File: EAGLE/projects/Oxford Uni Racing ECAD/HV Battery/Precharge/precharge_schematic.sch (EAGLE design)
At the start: 38 parts, among them IC1 TLV313QDCKRQ1, IC2 TLV313QDCKRQ1, U1 AMC1350QDWVRQ1AMC1350QDWVRQ1_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

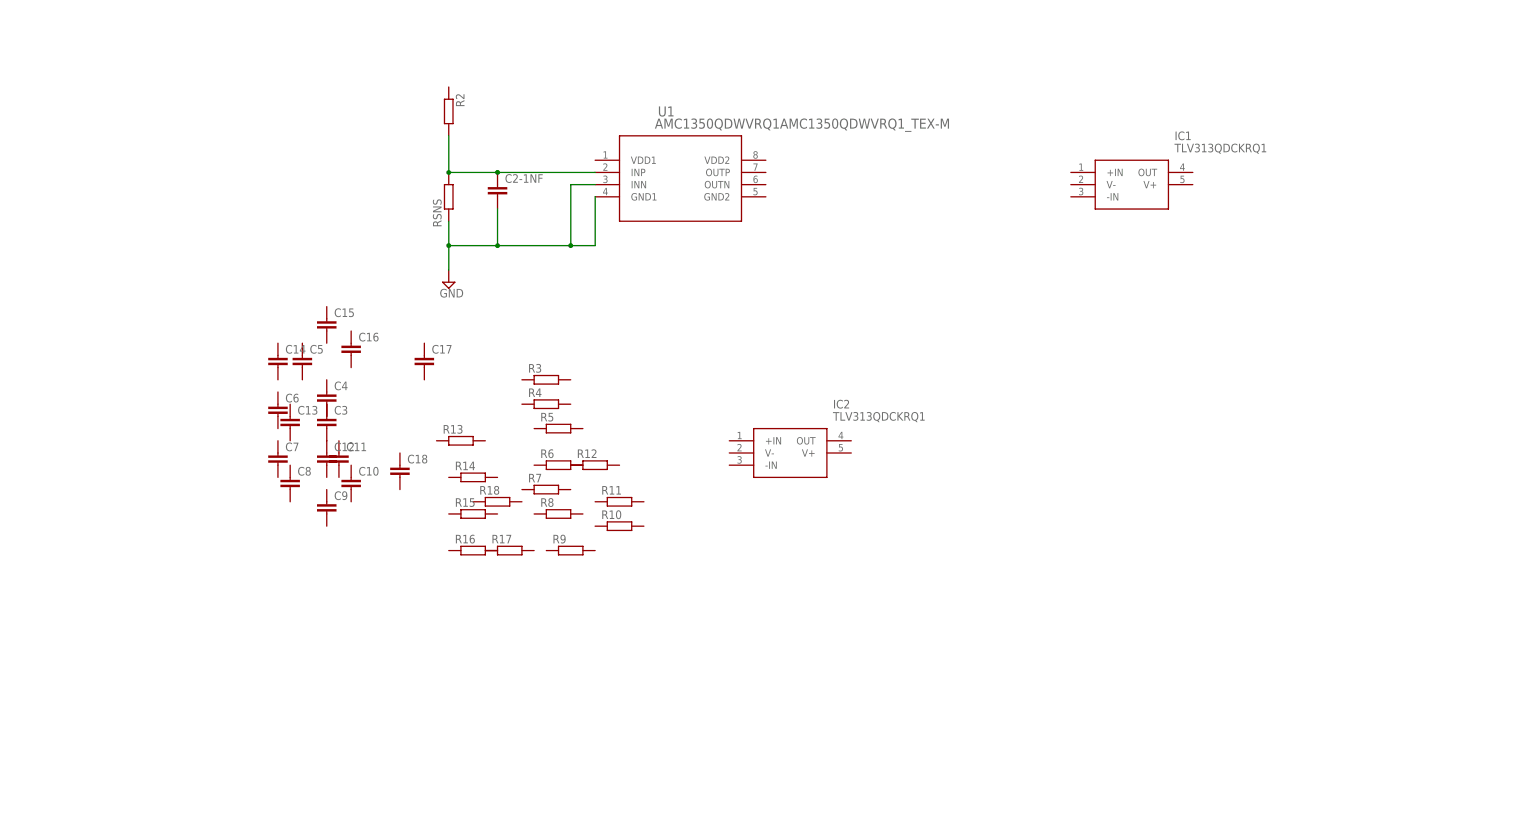
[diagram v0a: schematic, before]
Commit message: precharge board/ main board transfer
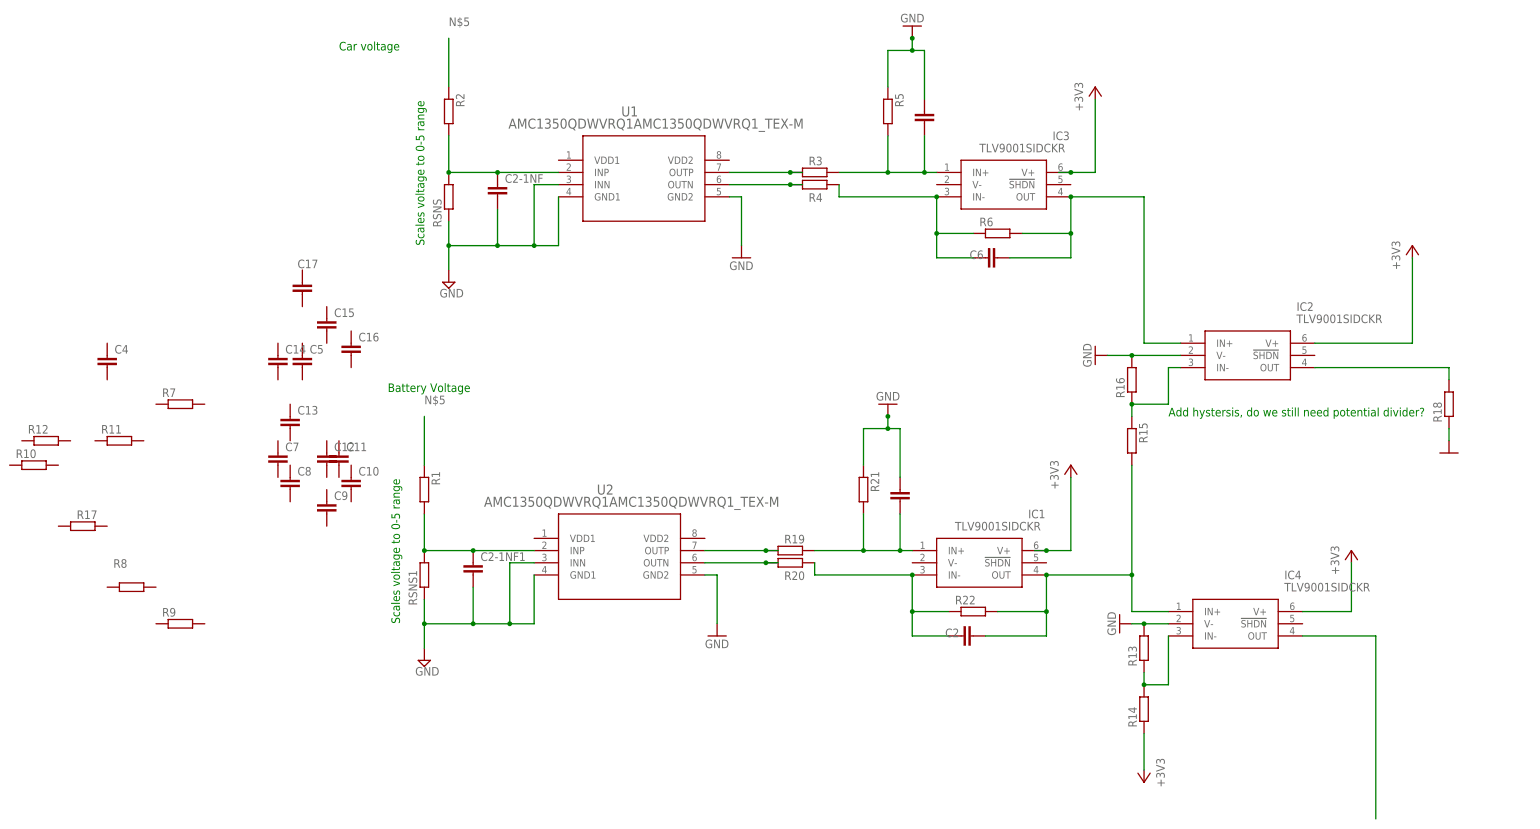
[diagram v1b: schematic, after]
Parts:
- removed C18: (no value), rcl:C-EUC0805
- added C1, C2, C2-1NF1: (no value), rcl:C-EUC0805
- added IC3, IC4: TLV9001SIDCKR, TLV9001SIDCKR:TLV9001SIDCKR
- added R1, R19, R20, R21, R22, RSNS1: (no value), rcl:R-EU_R0805
- added U2: AMC1350QDWVRQ1AMC1350QDWVRQ1_TEX-M, AMC1350QDWVRQ1:AMC1350QDWVRQ1AMC1350QDWVRQ1_TEX-M
- IC1, IC2: value TLV313QDCKRQ1 -> TLV9001SIDCKR; device TLV313QDCKRQ1:TLV313QDCKRQ1 -> TLV9001SIDCKR:TLV9001SIDCKR
- U1: MANUFACTURER_PART_NUMBER (none) -> AMC1350
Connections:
- new net +3V3: IC1.V+, IC2.V+, IC3.V+, IC4.V+, R14.1
- new net N$10: R19.1, U2.OUTP
- new net N$11: R20.1, U2.OUTN
- new net N$12: C1.2, IC1.IN+, R19.2, R21.2
- new net N$13: C1.1, R21.1
- new net N$14: C2.1, IC1.IN-, R20.2, R22.1
- new net N$15: IC2.OUT, R18.2
- new net N$16: C2.2, IC1.OUT, IC2.IN-, IC4.IN+, R15.1, R15.2, R16.1, R22.2
- new net N$17: IC4.IN-, R13.1, R14.2
- new net N$19: IC4.OUT
- new net N$3: R4.1, U1.OUTN
- new net N$4: R3.1, U1.OUTP
- new net N$5: R1.1, R2.1
- new net N$6: C3.2, IC3.IN+, R3.2, R5.2
- new net N$7: C6.1, IC3.IN-, R4.2, R6.1
- new net N$8: C6.2, IC2.IN+, IC3.OUT, R6.2
- new net N$9: C2-1NF1.1, R1.2, RSNS1.2, U2.INP
- net GND: now also C2-1NF1.2, IC2.V-, IC4.V-, R13.2, R16.2, R18.1, RSNS1.1, U1.GND2, U2.GND1, U2.GND2, U2.INN
- net N$2: now also C3.1, R5.1; no longer C12.1, C3.2
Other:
- note added: "Add hystersis, do we still need potential divider?"
- note added: "Battery Voltage"
- note added: "Car voltage"
- note added: "Scales voltage to 0-5 range"
- moved on the sheet: C17, C4, C6, R10, R11, R12, R13, R14, R15, R16, R17, R18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

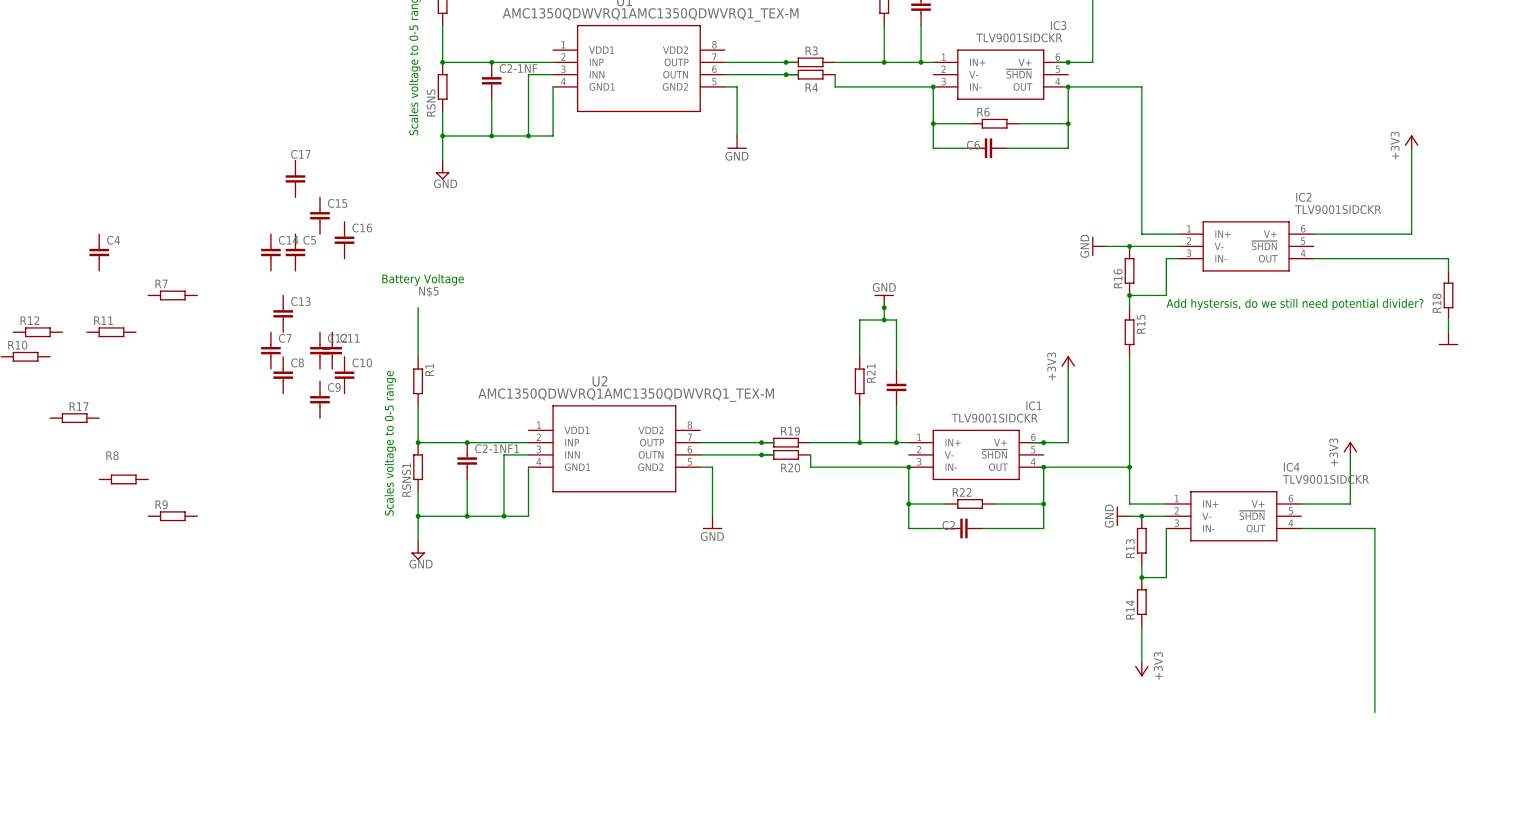
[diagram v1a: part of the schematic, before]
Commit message: Precharge for aminah
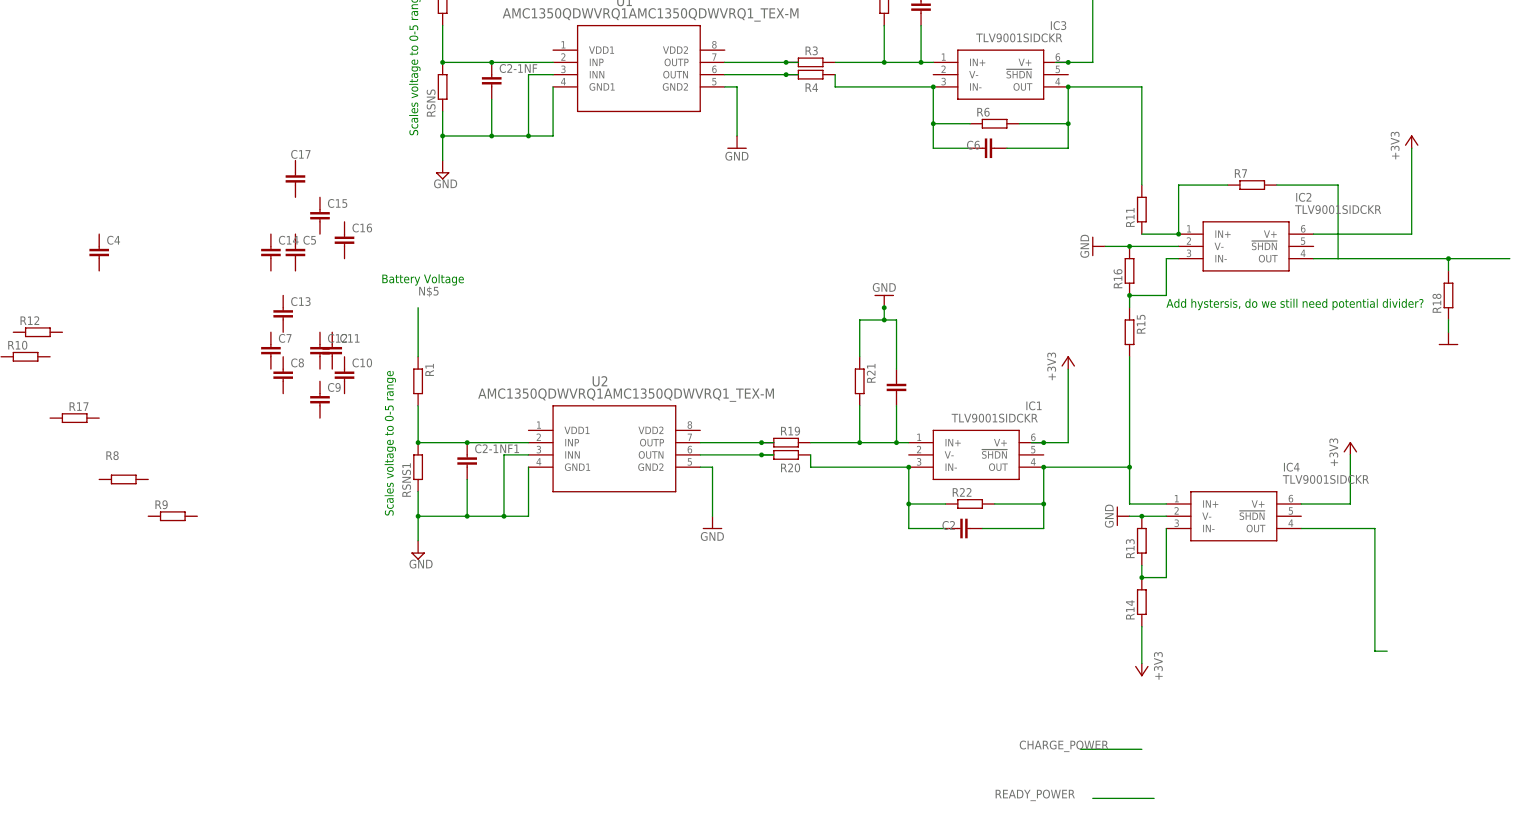
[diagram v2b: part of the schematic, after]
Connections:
- new net N$18: IC2.IN+, R11.1, R7.1
- net N$15: now also R7.2
- net N$8: now also R11.2; no longer IC2.IN+
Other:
- moved on the sheet: R11, R7
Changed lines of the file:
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@@
 <attribute name="VALUE" x="92.71" y="72.898" size="1.778" layer="96"/>
 </instance>
-<instance part="R7" gate="G$1" x="-73.66" y="40.64" smashed="yes">
-<attribute name="NAME" x="-77.47" y="42.1386" size="1.778" layer="95"/>
-<attribute name="VALUE" x="-77.47" y="37.338" size="1.778" layer="96"/>
+<instance part="R7" gate="G$1" x="149.86" y="63.5" smashed="yes">
+<attribute name="NAME" x="146.05" y="64.9986" size="1.778" layer="95"/>
+<attribute name="VALUE" x="146.05" y="60.198" size="1.778" layer="96"/>
 </instance>
 <instance part="R8" gate="G$1" x="-83.82" y="2.54" smashed="yes">
@@
 <attribute name="VALUE" x="-107.95" y="24.638" size="1.778" layer="96"/>
 </instance>
-<instance part="R11" gate="G$1" x="-86.36" y="33.02" smashed="yes">
-<attribute name="NAME" x="-90.17" y="34.5186" size="1.778" layer="95"/>
-<attribute name="VALUE" x="-90.17" y="29.718" size="1.778" layer="96"/>
+<instance part="R11" gate="G$1" x="127" y="58.42" smashed="yes" rot="R90">
+<attribute name="NAME" x="125.5014" y="54.61" size="1.778" layer="95" rot="R90"/>
+<attribute name="VALUE" x="130.302" y="54.61" size="1.778" layer="96" rot="R90"/>
 </instance>
 <instance part="R12" gate="G$1" x="-101.6" y="33.02" smashed="yes">
@@
 <wire x1="101.6" y1="76.2" x2="111.76" y2="76.2" width="0.1524" layer="91"/>
 <junction x="111.76" y="76.2"/>
+<pinref part="R11" gate="G$1" pin="2"/>
 <wire x1="111.76" y1="83.82" x2="127" y2="83.82" width="0.1524" layer="91"/>
+<wire x1="127" y1="83.82" x2="127" y2="63.5" width="0.1524" layer="91"/>
 <junction x="111.76" y="83.82"/>
-<pinref part="IC2" gate="G$1" pin="IN+"/>
-<wire x1="127" y1="83.82" x2="127" y2="53.34" width="0.1524" layer="91"/>
-<wire x1="127" y1="53.34" x2="134.62" y2="53.34" width="0.1524" layer="91"/>
 </segment>
 </net>
@@
 <segment>
 <pinref part="IC2" gate="G$1" pin="OUT"/>
-<wire x1="162.56" y1="48.26" x2="190.5" y2="48.26" width="0.1524" layer="91"/>
+<wire x1="162.56" y1="48.26" x2="167.64" y2="48.26" width="0.1524" layer="91"/>
+<wire x1="167.64" y1="48.26" x2="190.5" y2="48.26" width="0.1524" layer="91"/>
 <wire x1="190.5" y1="48.26" x2="190.5" y2="45.72" width="0.1524" layer="91"/>
 <pinref part="R18" gate="G$1" pin="2"/>
+<wire x1="167.64" y1="48.26" x2="167.64" y2="63.5" width="0.1524" layer="91"/>
+<wire x1="167.64" y1="63.5" x2="154.94" y2="63.5" width="0.1524" layer="91"/>
+<pinref part="R7" gate="G$1" pin="2"/>
+<wire x1="190.5" y1="48.26" x2="203.2" y2="48.26" width="0.1524" layer="91"/>
+<junction x="190.5" y="48.26"/>
 </segment>
 </net>
@@
 <pinref part="IC4" gate="G$1" pin="OUT"/>
 <wire x1="160.02" y1="-7.62" x2="175.26" y2="-7.62" width="0.1524" layer="91"/>
-<wire x1="175.26" y1="-7.62" x2="175.26" y2="-45.72" width="0.1524" layer="91"/>
-</segment>
-</net>
+<wire x1="175.26" y1="-7.62" x2="175.26" y2="-33.02" width="0.1524" layer="91"/>
+<wire x1="175.26" y1="-33.02" x2="177.8" y2="-33.02" width="0.1524" layer="91"/>
+</segment>
+</net>
+<net name="N$18" class="0">
+<segment>
+<pinref part="IC2" gate="G$1" pin="IN+"/>
+<pinref part="R7" gate="G$1" pin="1"/>
+<wire x1="144.78" y1="63.5" x2="134.62" y2="63.5" width="0.1524" layer="91"/>
+<wire x1="134.62" y1="63.5" x2="134.62" y2="53.34" width="0.1524" layer="91"/>
+<junction x="134.62" y="53.34"/>
+<wire x1="127" y1="53.34" x2="134.62" y2="53.34" width="0.1524" layer="91"/>
+<pinref part="R11" gate="G$1" pin="1"/>
+</segment>
+</net>
+<net name="CHARGE_POWER" class="0">
+<segment>
+<wire x1="114.3" y1="-53.34" x2="127" y2="-53.34" width="0.1524" layer="91"/>
+<label x="101.6" y="-53.34" size="1.778" layer="95"/>
+</segment>
+</net>
+<net name="READY_POWER" class="0">
+<segment>
+<wire x1="116.84" y1="-63.5" x2="129.54" y2="-63.5" width="0.1524" layer="91"/>
+<label x="96.52" y="-63.5" size="1.778" layer="95"/>
+</segment>
+</net>

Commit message: Updates to precharge schematic
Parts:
- removed C12, C15, C16, C17: (no value), rcl:C-EUC0805
- added IC10: 74HC1G86GW-Q100H, 74HC1G86GW-Q100H:74HC1G86GW-Q100H
- added IC11: 74LVC1G32GV,125, 74LVC1G32GV_125:74LVC1G32GV,125
- added IC5, IC6, IC7, IC8: LT1129CS8-3.3#PBF, LT1129CS8-3.3#PBF:LT1129CS8-3.3#PBF
- added IC9: 74AHC1G08GV,125, 74AHC1G08GV_125:74AHC1G08GV,125
- added J1: T816108A1S102CEU, T816108A1S102CEU:T816108A1S102CEU
- added PS1, PS2: PDSE1-S12-S5-M-TR, PDSE1-S12-S5-M-TR:PDSE1-S12-S5-M-TR
- added Q1, Q2: BSS138, BSS138:BSS138
- added R23, R24: (no value), rcl:R-EU_R0805
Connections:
- removed net N$5 (its old number): R1.1, R2.1
- new net +12V: IC7.VIN, IC8.VIN, Q2.D
- new net CHARGE_POWER: IC6.VIN
- new net N$13: C8.1, IC1.IN-, R20.2, R22.1
- new net N$20: C14.2
- new net N$21: C5.2
- new net N$22: C13.2, C7.2, PS2.+VOUT, R12.1, U1.VDD1
- new net N$23: PS2.0V, R10.2
- new net N$24: IC7.OUTPUT, PS2.VIN
- new net N$25: R10.1, R12.2
- new net N$26: C11.2
- new net N$27: C2.2
- new net N$28: C10.2, C9.2, PS1.+VOUT, R24.1, U2.VDD1
- new net N$29: PS1.0V, R23.2
- new net N$30: IC8.OUTPUT, PS1.VIN
- new net N$31: R23.1, R24.2
- new net N$32: IC10.A, IC6.OUTPUT
- new net N$33: IC10.B, IC5.OUTPUT
- new net N$34: IC10.Y, IC9.A
- new net N$35: IC9.Y, Q2.G
- new net N$36: IC6.GND_2, IC6.GND_3
- new net N$37: IC5.GND_2, IC5.GND_3
- new net N$38: IC11.Y, Q1.G
- new net N$40: J1.1, Q1.D
- new net READY_POWER: IC5.VIN
- net +3V3: now also C11.1, C14.1, C2.1, C5.1, IC10.VCC, IC11.VCC, IC9.VCC, U1.VDD2, U2.VDD2
- net GND: now also C10.1, C13.1, C7.1, C9.1, IC10.GND, IC11.GND, IC5.GND_1, IC6.GND_1, IC7.GND_1, IC7.GND_2, IC7.GND_3, IC8.GND_1, IC8.GND_2, IC8.GND_3, IC9.GND, PS1.GND, PS2.GND, Q1.S, Q2.S
- net N$14: now also C8.2, IC1.OUT, R22.2; no longer C2.1, IC1.IN-, R20.2, R22.1
- net N$15: now also IC11.A
- net N$16: no longer C2.2, IC1.OUT, R22.2
- net N$19: now also IC9.B
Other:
- note added: "Unreg DcDc, needs to be changed"
- note removed: "Battery Voltage"
- moved on the sheet: C10, C11, C13, C14, C2, C2-1NF1, C5, C7, C8, C9, IC1, R1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
